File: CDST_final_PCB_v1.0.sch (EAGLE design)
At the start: 51 parts, among them IC1 MIC_I2S_SPH0645, IC2 LM2596S, U1 AD8232ACPZ-R7

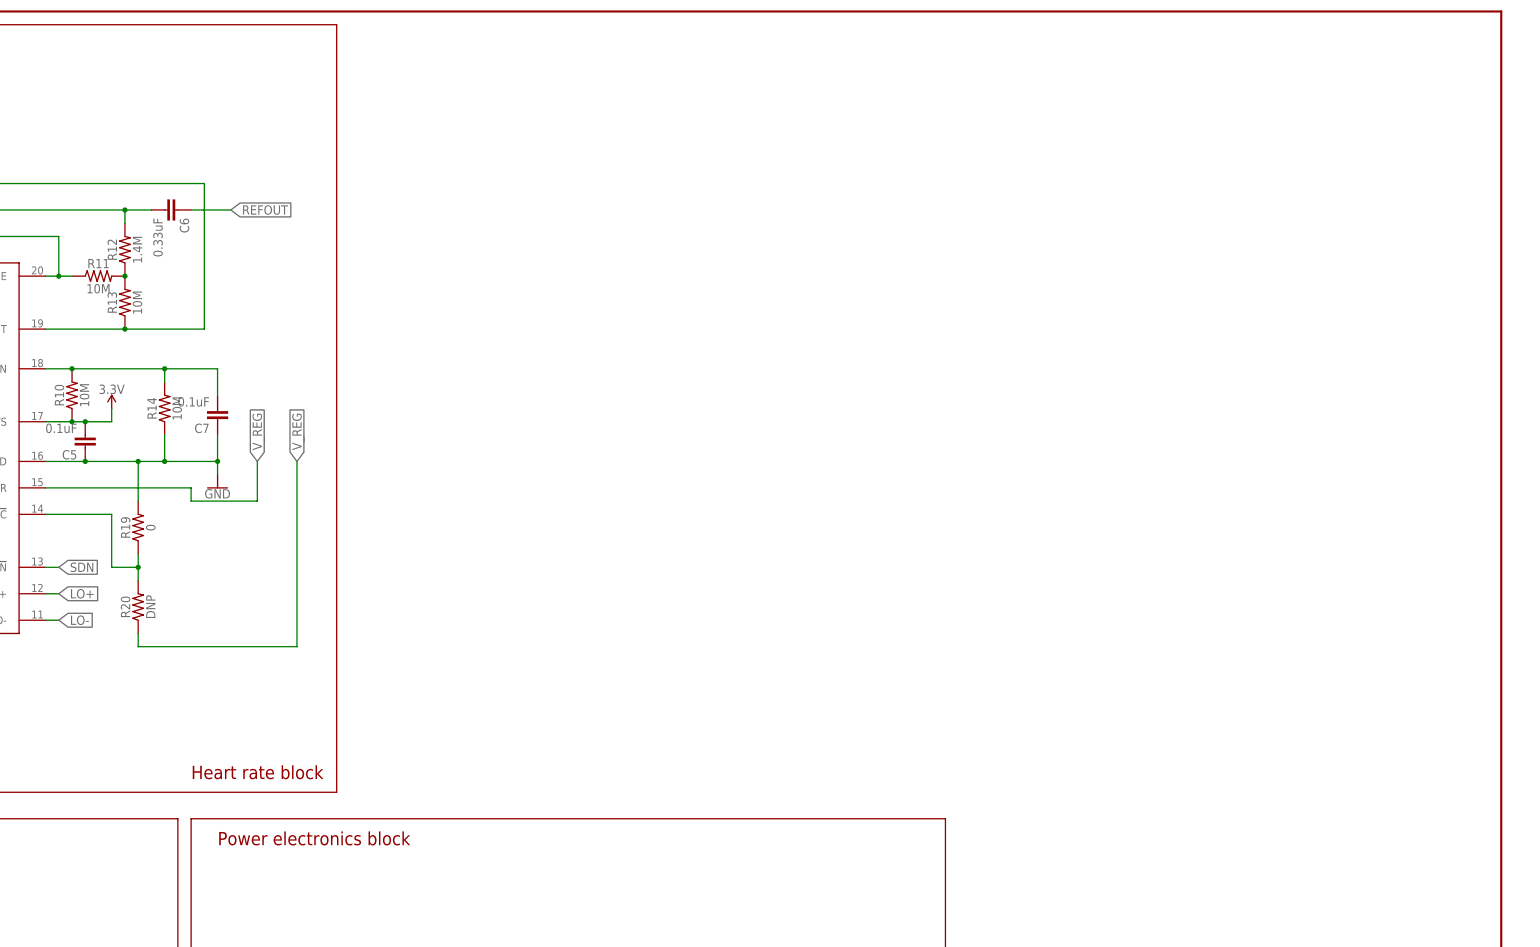
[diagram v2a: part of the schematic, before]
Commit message: added esp32
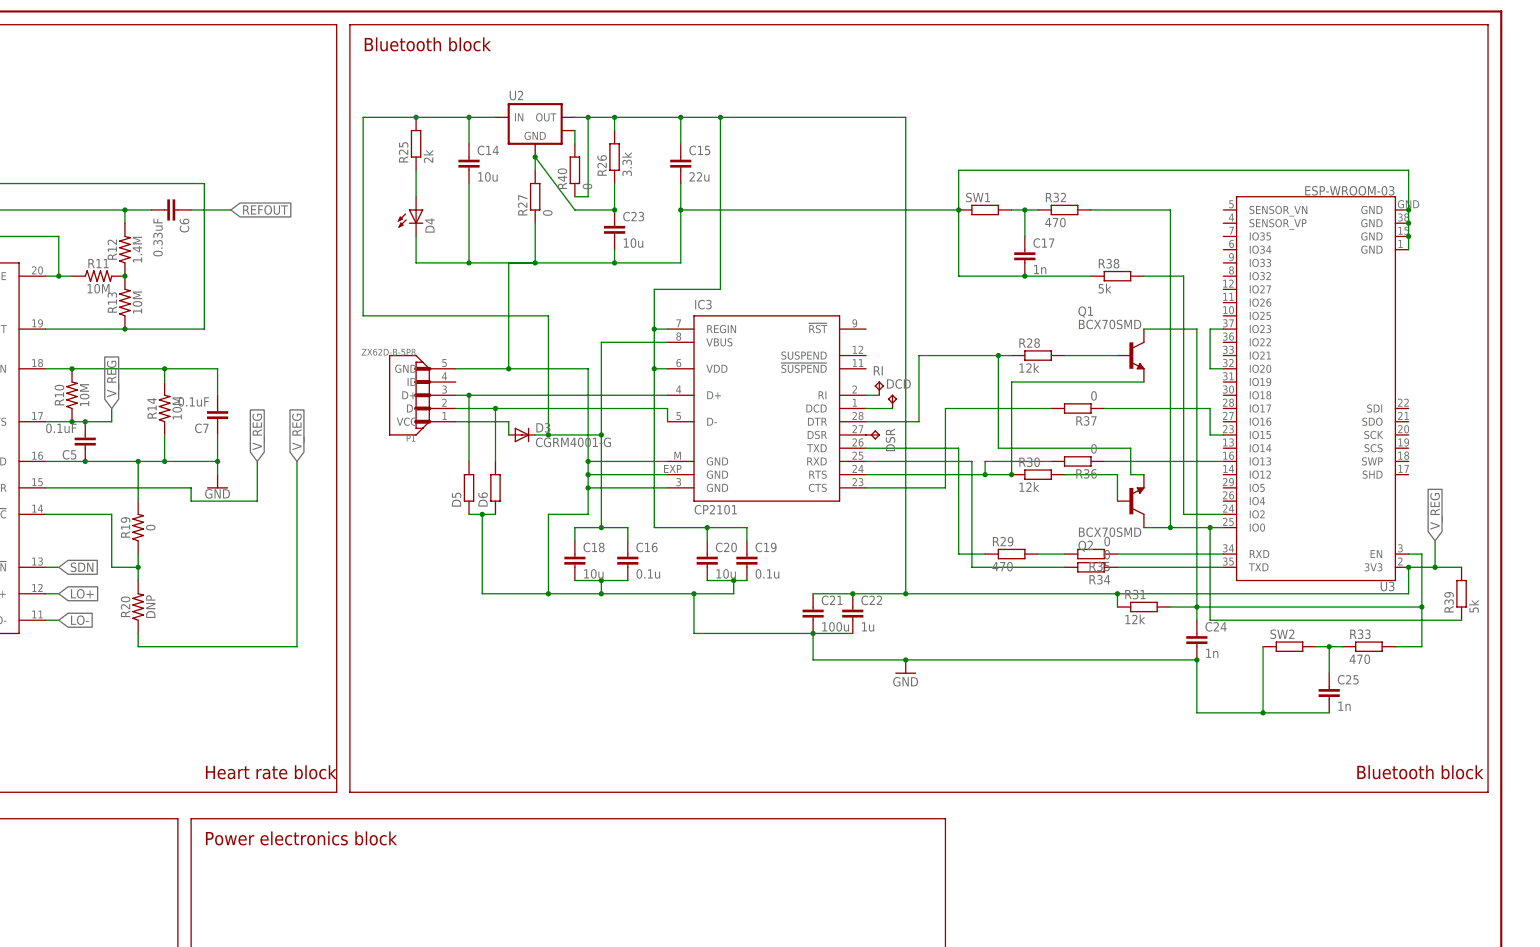
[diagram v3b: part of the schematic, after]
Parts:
- added C14, C18, C20, C23: 10u, eagle-ltspice:CC1206
- added C15: 22u, eagle-ltspice:CC1206
- added C16, C19: 0.1u, eagle-ltspice:CC1206
- added C17, C24, C25: 1n, eagle-ltspice:CC1206
- added C21: 100u, eagle-ltspice:CC1206
- added C22: 1u, eagle-ltspice:CC1206
- added D3: CGRM4001-G, diode:CGRM4001-G
- added D4: (no value), led:LEDCHIPLED_0805
- added D5, D6: (no value), eagle-ltspice:RR0402
- added DCD, DSR, RI: TPB2,54, testpad:TPB2,54
- added IC3: CP2101, silabs:CP2101
- added P1: ZX62D-B-5P8, ZX62D-B-5P8:ZX62D-B-5P8
- added Q1, Q2: BCX70SMD, transistor:BCX70SMD
- added R25: 2k, eagle-ltspice:RR1206
- added R26: 3.3k, eagle-ltspice:RR1206
- added R27, R34, R35, R36, R37, R40: 0, eagle-ltspice:RR1206
- added R28, R30, R31: 12k, eagle-ltspice:RR1206
- added R29, R32, R33: 470, eagle-ltspice:RR1206
- added R38, R39: 5k, eagle-ltspice:RR1206
- added SW1, SW2: (no value), eagle-ltspice:RR2010
- added U2: (no value), bt_regulator:LM1117-SOT223
- added U3: ESP-WROOM-03, esp32:ESP-WROOM-03
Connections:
- removed net VCC: C5.2, R10.1, U1.+VS
- new net DCD: DCD.TP, IC3.DCD
- new net HEATSINK: R40.2, U2.HEATSINK
- new net N$20: C14.1, C16.1, C18.1, D3.C, IC3.VBUS, R25.2, U2.VIN
- new net N$23: D5.2, IC3.D+, P1.D+
- new net N$24: D6.2, IC3.D-, P1.D-
- new net N$25: D3.A, P1.VCC
- new net N$26: Q1.B, R28.2
- new net N$27: IC3.RTS, Q1.E, R30.1, R36.2
- new net N$28: IC3.DTR, Q2.E, R28.1
- new net N$29: C24.1, Q1.C, R31.2, R33.2, U3.EN
- new net N$30: IC3.RXD, R34.2
- new net N$31: IC3.TXD, R29.1
- new net N$33: U3.IO20, U3.IO23
- new net N$34: C25.1, R33.1, SW2.2
- new net N$35: C17.1, R32.1, SW1.2
- new net N$36: Q2.C, R32.2, R39.1, U3.IO0
- new net N$37: R38.2, U3.IO2
- new net N$38: R34.1, U3.TXD
- new net N$39: R29.2, R35.2
- new net N$40: R35.1, U3.RXD
- new net N$41: R36.1, U3.IO13
- new net N$42: IC3.CTS, R37.2
- new net N$43: R37.1, U3.IO15
- new net N$44: Q2.B, R30.2
- new net N$45: IC3.RI, RI.TP
- new net N$46: DSR.TP, IC3.DSR
- new net N$9: D4.A, R25.1
- net GND: now also C14.2, C15.2, C16.2, C17.2, C18.2, C19.2, C20.2, C21.2, C22.2, C23.1, C23.2, C24.2, C25.2, D4.C, D5.1, D6.1, IC3.GND, IC3.GND@EXP, IC3.GND@M, P1.GND, R26.1, R27.1, R27.2, R38.1, SW1.1, SW2.1, U2.GND, U3.GND, U3.GND@1, U3.GND@15, U3.GND@38
- net V_REG: now also C15.1, C19.1, C20.1, C21.1, C22.1, C5.2, IC3.REGIN, IC3.VDD, R10.1, R26.2, R31.1, R39.2, R40.1, U1.+VS, U2.VOUT, U3.3V3
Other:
- note added: "Bluetooth block"
